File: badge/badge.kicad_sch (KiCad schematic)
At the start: 27 parts, among them J1 Conn_01x03_Pin, SW1 SW_Push, Y2 1.843

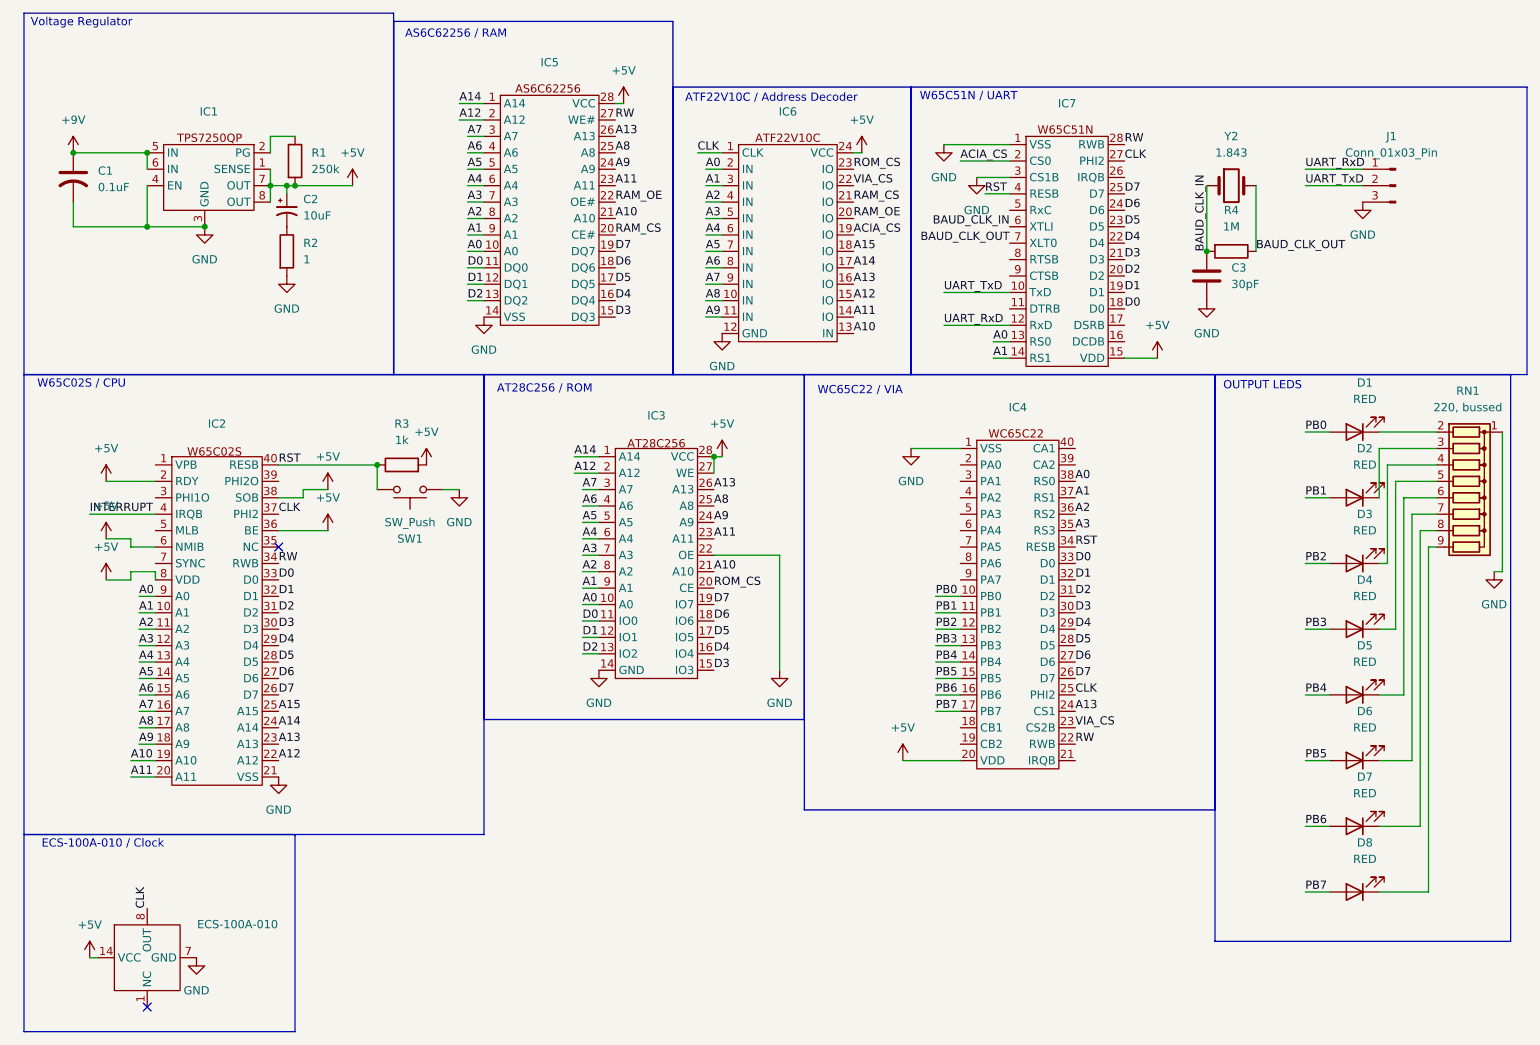
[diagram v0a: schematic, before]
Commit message: Assign various footprints and fix a few issues
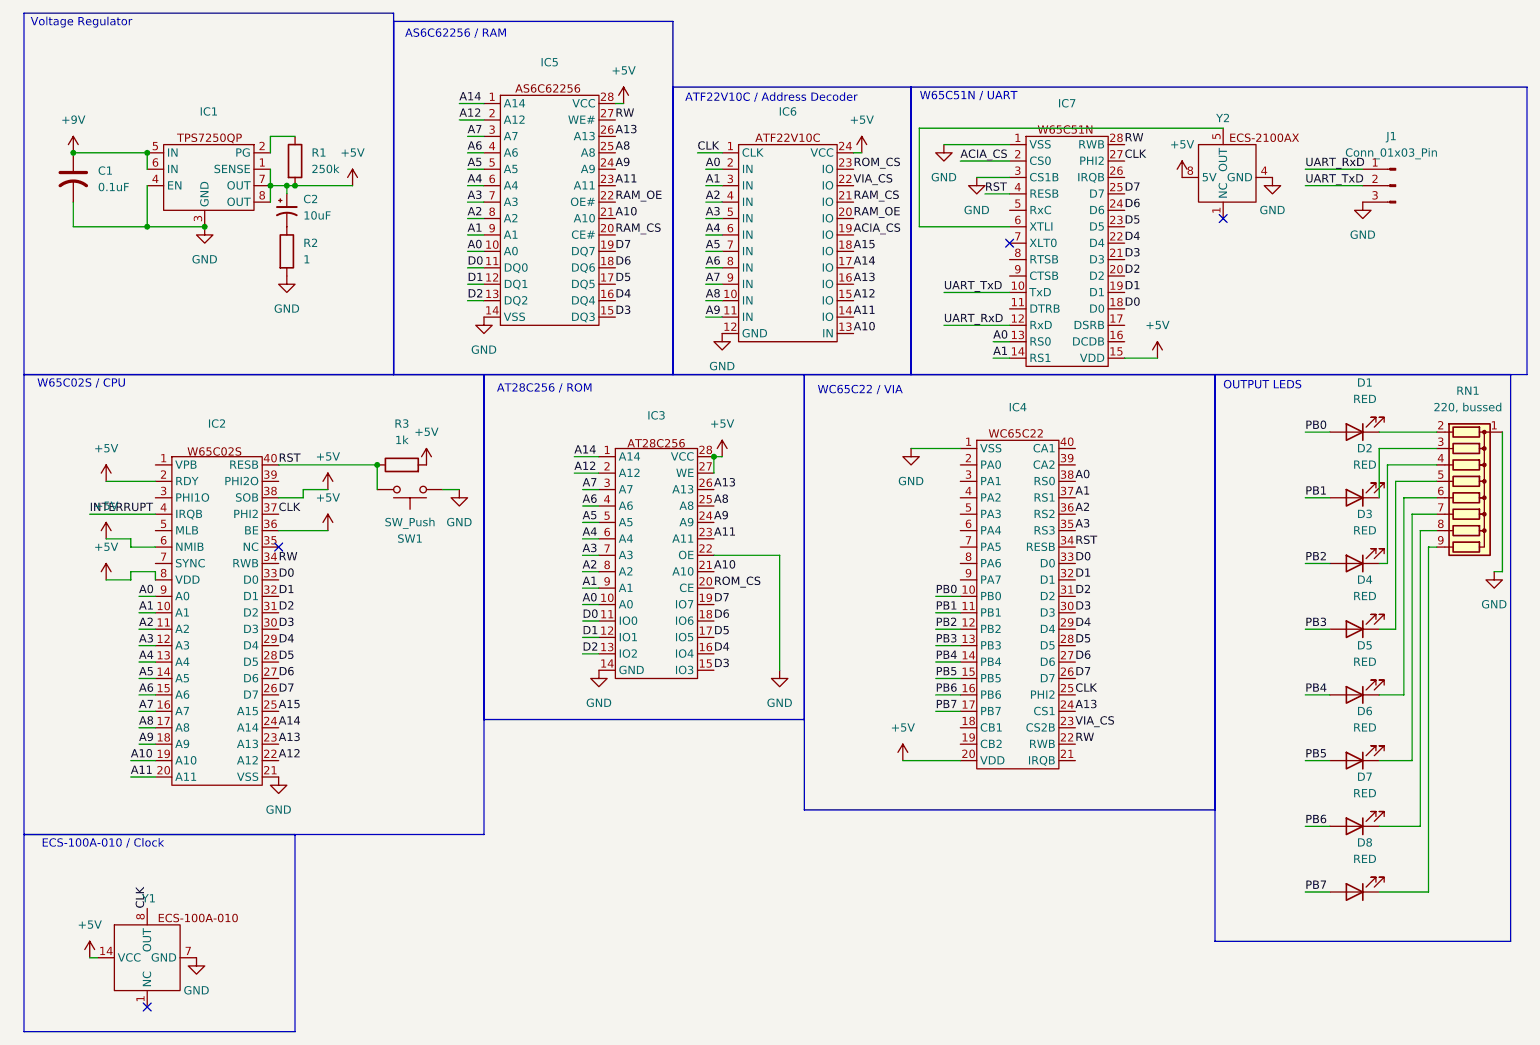
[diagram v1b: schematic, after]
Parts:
- removed C3: 30pF, symbol Device:C
- removed R4: 1M, symbol Device:R
- removed Y2: 1.843, symbol Device:Crystal
- added Y2: ~, symbol 6502ConferenceBadge:ECS-2100AX-1.8432
- C1: footprint (none) -> Capacitor_THT:CP_Radial_Tantal_D5.5mm_P2.50mm
- IC1: footprint (none) -> Package_DIP:DIP-8-16_W7.62mm_Socket
- IC2, IC4: footprint (none) -> Package_DIP:DIP-40_W15.24mm_Socket
- IC3, IC5, IC7: footprint (none) -> Package_DIP:DIP-28_W15.24mm_Socket
- IC6: footprint (none) -> Package_DIP:DIP-24_W7.62mm_Socket
- J1: footprint (none) -> Connector_PinHeader_2.54mm:PinHeader_1x03_P2.54mm_Horizontal
- R1: footprint (none) -> Resistor_THT:R_Axial_DIN0411_L9.9mm_D3.6mm_P7.62mm_Vertical
- R2: footprint (none) -> Resistor_THT:R_Axial_DIN0516_L15.5mm_D5.0mm_P20.32mm_Horizontal
- R3: footprint (none) -> Resistor_THT:R_Axial_DIN0309_L9.0mm_D3.2mm_P12.70mm_Horizontal
- renumbered ECS-100A-010 to Y1
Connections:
- net +5V: now also Y2.8 (5V)
- net GND: now also Y2.4 (GND)
- net BAUD_CLK_IN: no longer names the net of IC7.6 (XTLI)
- net BAUD_CLK_IN: now also Y2.5 (OUT)
- net BAUD_CLK_OUT: no longer names the net of IC7.7 (XLT0)
- no-connect marks 2 -> 4

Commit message: Assign some footprints
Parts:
- C2: footprint (none) -> Capacitor_THT:CP_Axial_L10.0mm_D6.0mm_P15.00mm_Horizontal
- D1, D2, D3, D4, D5, D6, D7, D8: footprint (none) -> LED_THT:LED_D5.0mm
- SW1: footprint (none) -> Button_Switch_THT:SW_PUSH_6mm
- Y1: footprint (none) -> ECS-100A-010:ECS100A010
- Y2: footprint (none) -> ECS-2100AX:ECS2100AX18432MHZ
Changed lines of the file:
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@@
 			)
 		)
-		(property "Footprint" ""
+		(property "Footprint" "Capacitor_THT:CP_Axial_L10.0mm_D6.0mm_P15.00mm_Horizontal"
 			(at 52.07 41.91 0)
 			(effects
@@
 			)
 		)
-		(property "Footprint" ""
+		(property "Footprint" "LED_THT:LED_D5.0mm"
 			(at 217.17 147.32 0)
 			(effects
@@
 			)
 		)
-		(property "Footprint" ""
+		(property "Footprint" "Button_Switch_THT:SW_PUSH_6mm"
 			(at 71.12 90.17 0)
 			(effects
@@
 			)
 		)
-		(property "Footprint" ""
+		(property "Footprint" "LED_THT:LED_D5.0mm"
 			(at 217.17 76.2 0)
 			(effects
@@
 			)
 		)
-		(property "Footprint" ""
+		(property "Footprint" "ECS-100A-010:ECS100A010"
 			(at 30.48 148.59 0)
 			(effects
@@
 			)
 		)
-		(property "Footprint" ""
+		(property "Footprint" "ECS-2100AX:ECS2100AX18432MHZ"
 			(at 196.85 27.94 0)
 			(effects
@@
 			)
 		)
-		(property "Footprint" ""
+		(property "Footprint" "LED_THT:LED_D5.0mm"
 			(at 217.17 116.84 0)
 			(effects
@@
 			)
 		)
-		(property "Footprint" ""
+		(property "Footprint" "LED_THT:LED_D5.0mm"
 			(at 217.17 106.68 0)
 			(effects
@@
 			)
 		)
-		(property "Footprint" ""
+		(property "Footprint" "LED_THT:LED_D5.0mm"
 			(at 217.17 137.16 0)
 			(effects
@@
 			)
 		)
-		(property "Footprint" ""
+		(property "Footprint" "LED_THT:LED_D5.0mm"
 			(at 217.17 127 0)
 			(effects
@@
 			)
 		)
-		(property "Footprint" ""
+		(property "Footprint" "LED_THT:LED_D5.0mm"
 			(at 217.17 96.52 0)
 			(effects
@@
 			)
 		)
-		(property "Footprint" ""
+		(property "Footprint" "LED_THT:LED_D5.0mm"
 			(at 217.17 86.36 0)
 			(effects

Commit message: Layout outputs
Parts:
- IC1: footprint Package_DIP:DIP-8-16_W7.62mm_Socket -> Package_DIP:DIP-8_W7.62mm_Socket
- J1: footprint Connector_PinHeader_2.54mm:PinHeader_1x03_P2.54mm_Horizontal -> Connector_PinHeader_2.54mm:PinHeader_1x03_P2.54mm_Vertical
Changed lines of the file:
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@@
 			)
 		)
-		(property "Footprint" "Connector_PinHeader_2.54mm:PinHeader_1x03_P2.54mm_Horizontal"
+		(property "Footprint" "Connector_PinHeader_2.54mm:PinHeader_1x03_P2.54mm_Vertical"
 			(at 223.52 38.1 0)
 			(effects
@@
 			)
 		)
-		(property "Footprint" "Package_DIP:DIP-8-16_W7.62mm_Socket"
+		(property "Footprint" "Package_DIP:DIP-8_W7.62mm_Socket"
 			(at 39.37 29.21 0)
 			(effects

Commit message: Some work on routing
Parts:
- added C3, C4, C5: 0.1uF, Capacitor_THT:CP_Radial_Tantal_D5.5mm_P2.50mm, symbol Device:C_US
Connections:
- net +5V: now also IC4.24 (CS1), C3.1, C4.1, C5.1
- net A13: no longer IC4.24 (CS1)
- net GND: now also C3.2, C4.2, C5.2
